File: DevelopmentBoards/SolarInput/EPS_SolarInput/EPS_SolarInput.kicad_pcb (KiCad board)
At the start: 2 copper layers, 26 parts, among them J1 2053380004, J2 Screw_Terminal_01x02, J3 Conn_01x02_Socket, J5 Conn_01x05_Pin, J6 Screw_Terminal_01x04, U1 INA232AIDDFR

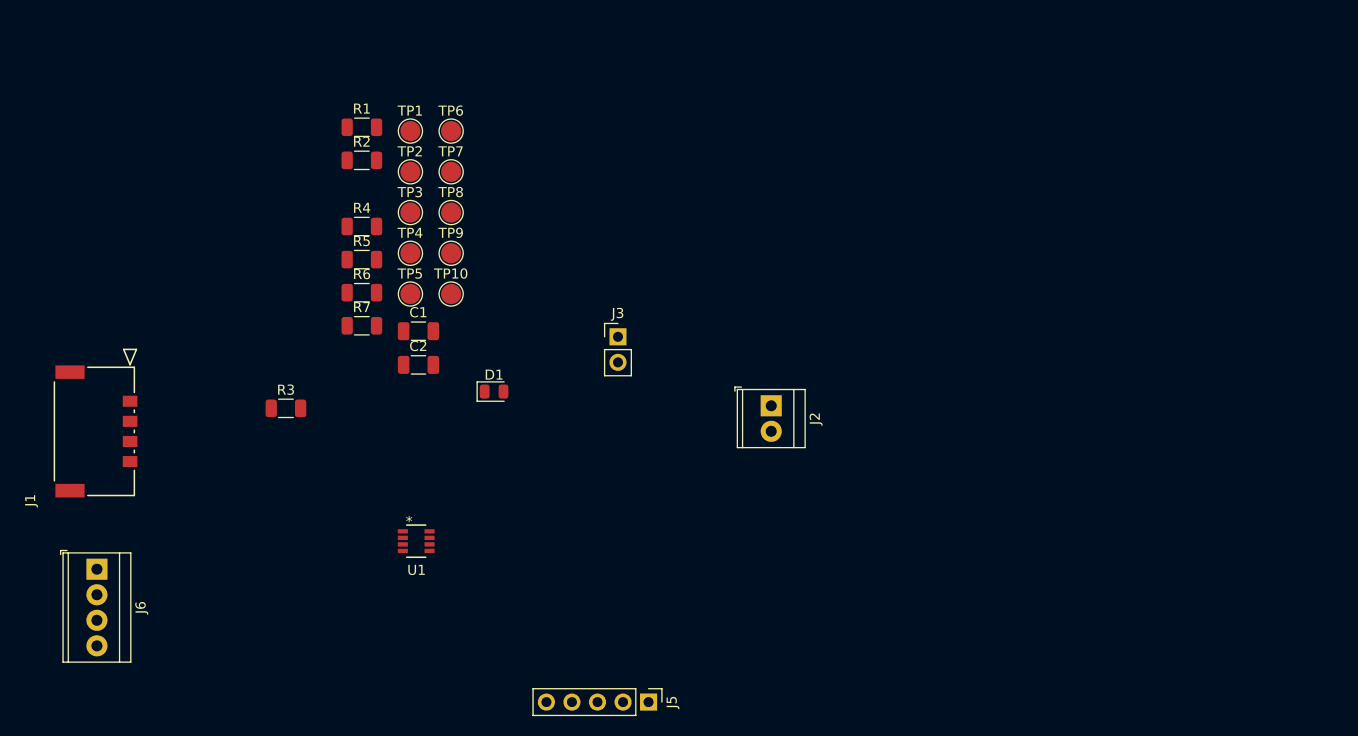
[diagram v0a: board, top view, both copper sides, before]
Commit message: Completed PCB Design for Solar Input Unit Development Board
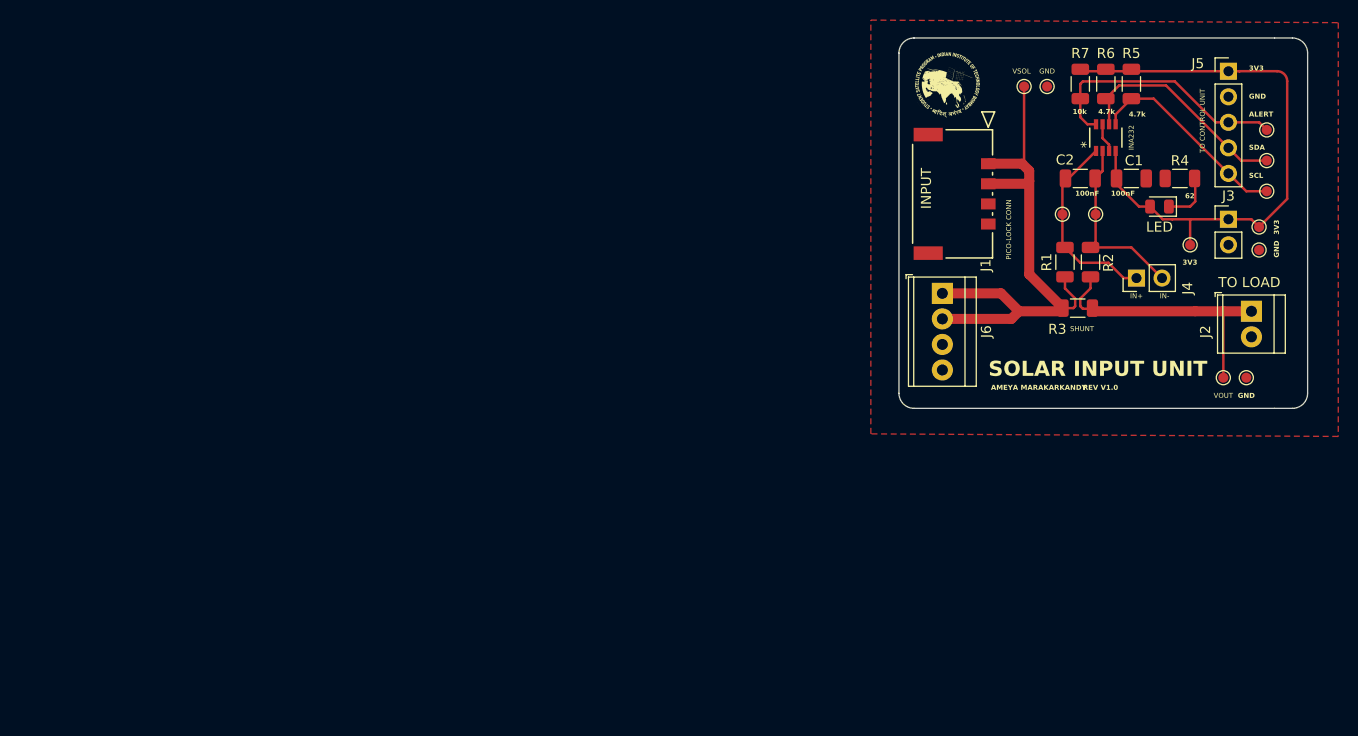
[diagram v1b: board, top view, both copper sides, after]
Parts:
- added G***: LOGO, Logo:IITBSSP_Logo, F.Cu at (126.5, 89.7)
- added GND: TestPoint, TestPoint:TestPoint_Pad_D1.0mm, F.Cu at (156.2, 118.9)
- added J4: Conn_01x02_Socket, Connector_PinHeader_2.54mm:PinHeader_1x02_P2.54mm_Vertical, F.Cu at (145.3, 109.0)
- added TP10: TestPoint, TestPoint:TestPoint_Pad_D1.0mm, F.Cu at (157.5, 103.9)
- C2: value 100nF -> C2
- TP1, TP2, TP3, TP4, TP5, TP6, TP7, TP8, TP9: footprint TestPoint:TestPoint_Pad_D2.0mm -> TestPoint:TestPoint_Pad_D1.0mm
- VOUT: renamed from TP10; footprint TestPoint:TestPoint_Pad_D2.0mm -> TestPoint:TestPoint_Pad_D1.0mm
- moved J1 88.6 mm to (130.6, 97.6)
- moved J6 88.4 mm to (126.0, 110.5)
- moved J5 85.2 mm to (154.4, 88.4), turned to 0 degrees
- moved TP8 81.5 mm to (158.2, 94.2)
- moved R4 81.5 mm to (149.6, 99.1)
- moved TP6 81.3 mm to (158.2, 100.3)
- moved TP7 81.1 mm to (158.2, 97.3)
- moved TP9 80.3 mm to (157.5, 106.2)
- moved INA232 79.5 mm to (142.2, 95.0), turned to 90 degrees
- moved R3 79.4 mm to (139.4, 112.0)
- moved R5 78.5 mm to (144.8, 89.7), turned to -90 degrees
- moved TP3 77.6 mm to (150.6, 105.7)
- moved VOUT 77.2 mm to (153.9, 118.9)
- moved R6 76.8 mm to (142.2, 89.7), turned to -90 degrees
- moved R7 75.4 mm to (139.7, 89.7), turned to -90 degrees
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- renumbered U1 to INA232
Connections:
- J1 pad 5: /VSOL -> GND
- J5 pad 3: /I2C_SCL -> /ALERT
- J5 pad 5: /ALERT -> /I2C_SCL
- TP1 pad 1: unconnected-(TP1-Pad1) -> /VSOL
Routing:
- net +3.3V: track 0.00 -> 58.7 mm
- net /VSOL: track 0.00 -> 56.8 mm
- net Net-(J2-Pin_1): track 0.00 -> 27.2 mm
- net /ALERT: track 0.00 -> 25.8 mm
- net /I2C_SDA: track 0.00 -> 22.3 mm
- net /I2C_SCL: track 0.00 -> 20.5 mm
- net Net-(J4-Pin_1): track 0.00 -> 19.6 mm
- net Net-(J4-Pin_2): track 0.00 -> 18.5 mm
- net Net-(D1-K): track 0.00 -> 5.14 mm
- net GND: track 0.00 -> 2.92 mm
- added copper zone on F.Cu, net GND
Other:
- board outline added: 40.6 x 36.8 mm
- board text added: "100nF"
- board text added: "10k"
- board text added: "3V3"
- board text added: "4.7k"
- board text added: "62"
- board text added: "ALERT"
- board text added: "AMEYA MARAKARKANDY"
- board text added: "GND"
- board text added: "IN+"
- board text added: "IN-"
- board text added: "INPUT"
- board text added: "PICO-LOCK CONN"
- board text added: "REV V1.0"
- board text added: "SCL"
- board text added: "SDA"
- board text added: "SHUNT"
- board text added: "SOLAR INPUT UNIT"
- board text added: "TO CONTROL UNIT"
- board text added: "TO LOAD"
